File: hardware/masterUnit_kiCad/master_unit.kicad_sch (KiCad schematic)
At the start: 13 parts, among them IC1 THVD8000DDFR, J1 Conn_01x03, J2 Conn_01x02, U1 DEV-15583

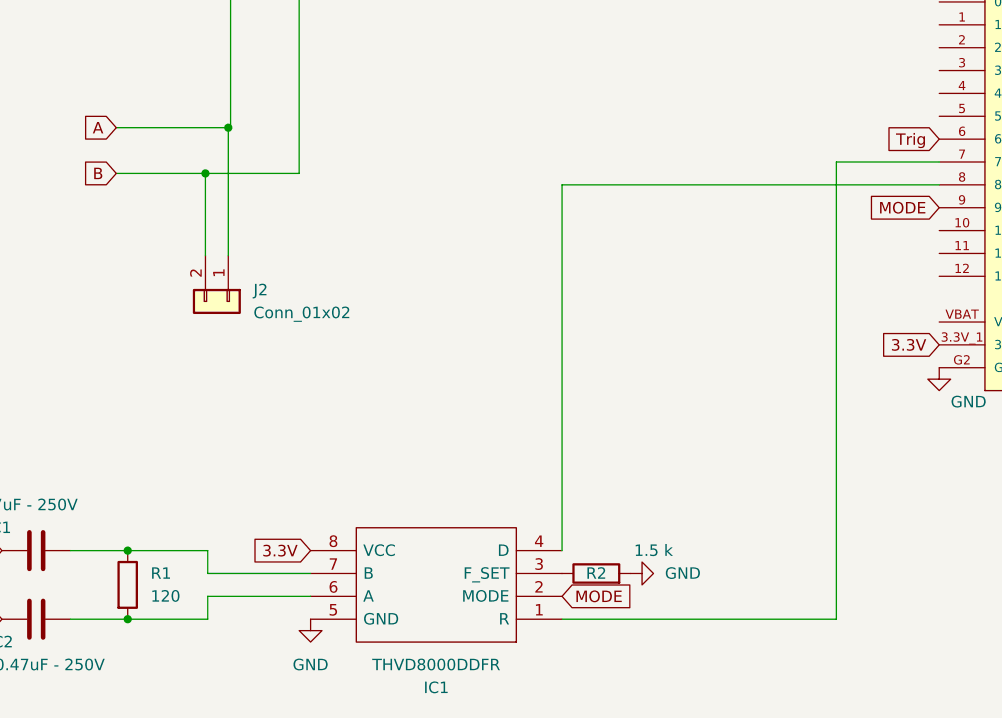
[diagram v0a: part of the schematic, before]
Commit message: Added LED to the master board
BLUE for power
RED for receiving data
GREEN for sending data
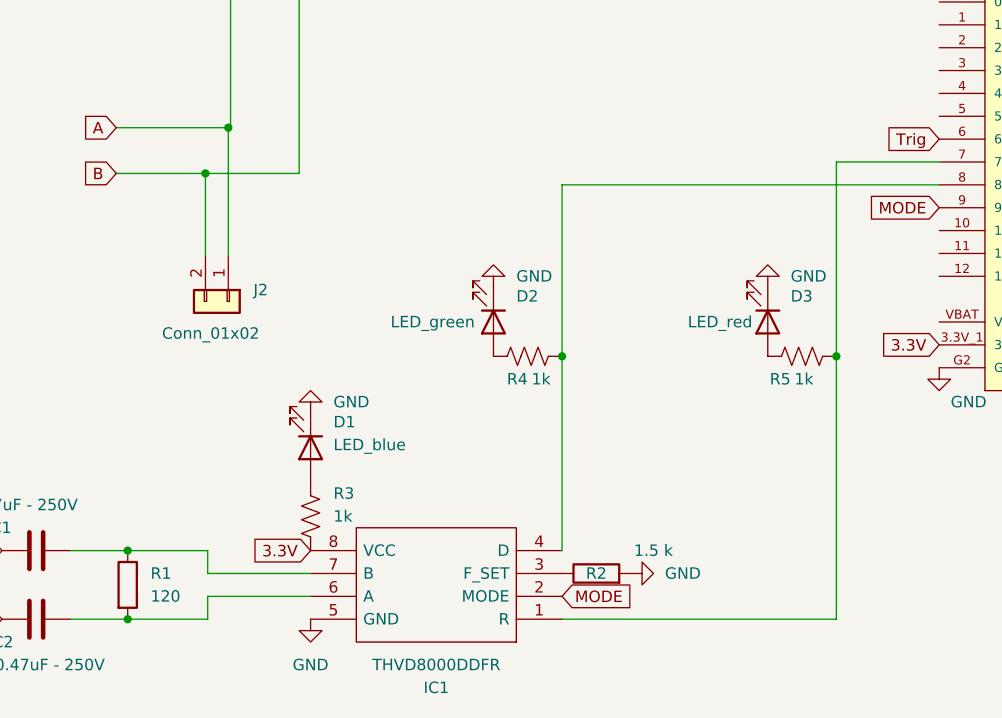
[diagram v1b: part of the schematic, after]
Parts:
- added D1: LED_blue, LED_SMD:LED_1206_3216Metric, symbol Device:LED
- added D2: LED_green, LED_SMD:LED_1206_3216Metric, symbol Device:LED
- added D3: LED_red, LED_SMD:LED_1206_3216Metric, symbol Device:LED
- added R3, R4, R5: 1k, Resistor_SMD:R_1206_3216Metric, symbol Device:R_US
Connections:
- net 3.3V: now also R3.2
- net GND: now also D1.1 (K), D2.1 (K), D3.1 (K)
- net at IC1.1 (R), U1.7: now also R5.2
- net at IC1.4 (D), U1.8: now also R4.2
- new net: D2.2 (A), R4.1
- new net: D3.2 (A), R5.1
- new net: D1.2 (A), R3.1

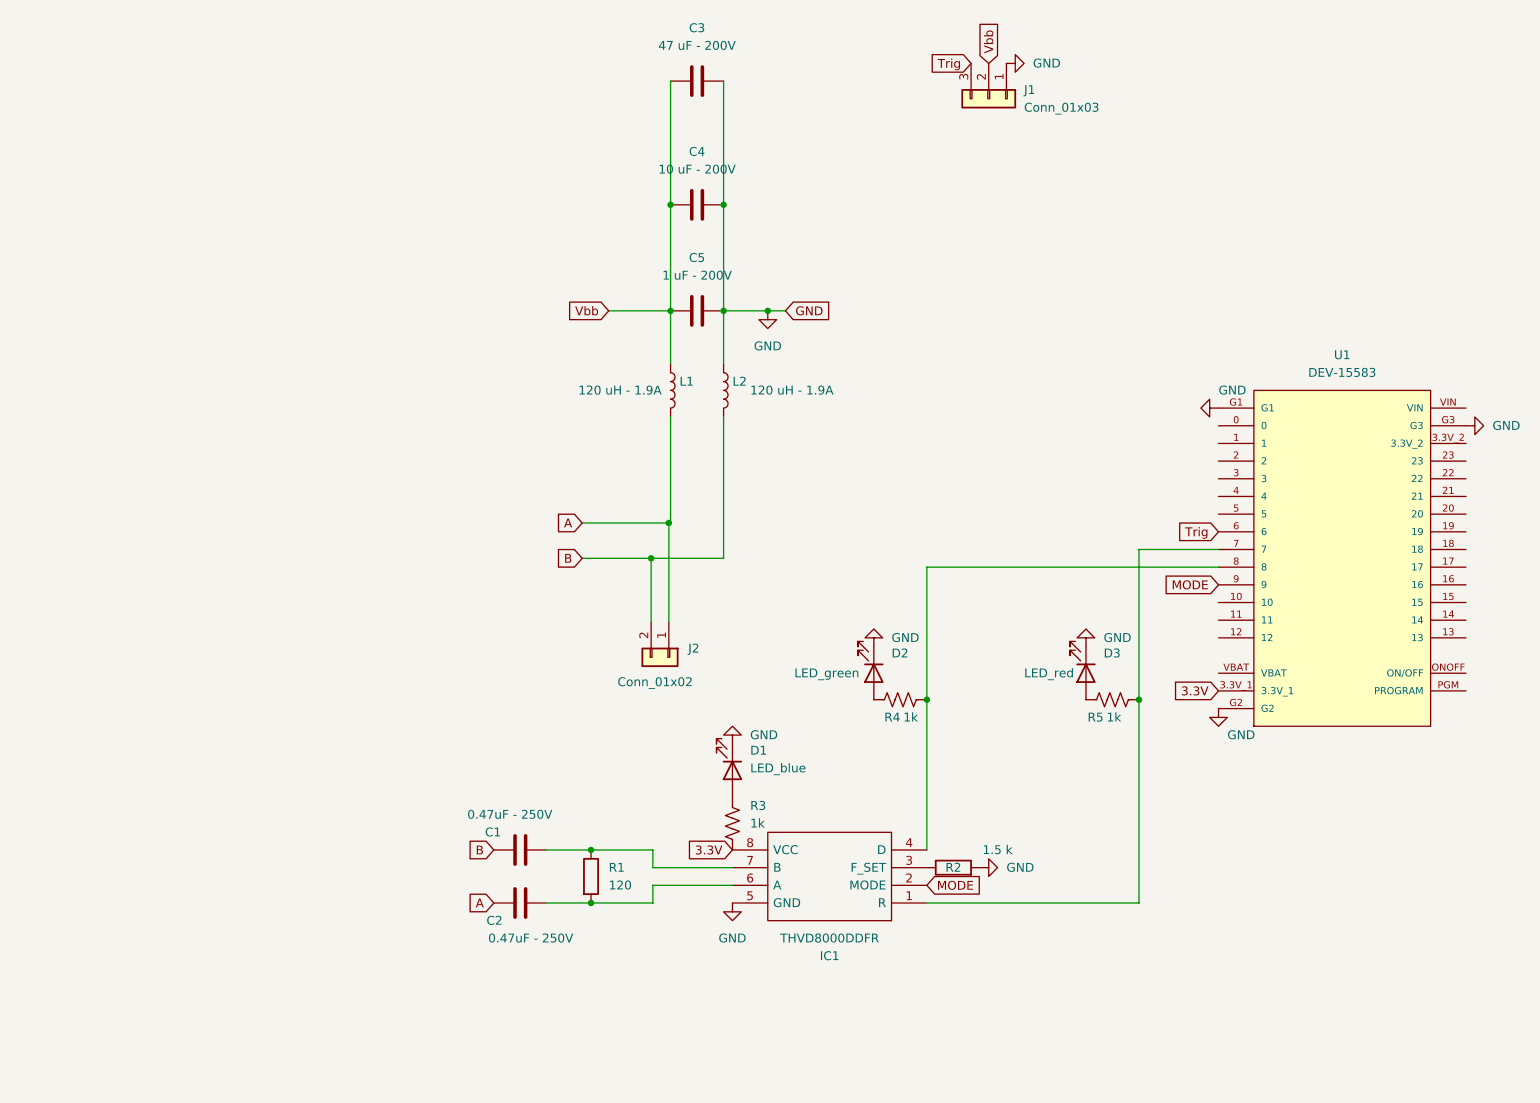
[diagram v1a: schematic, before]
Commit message: updated pcb layout with new LED
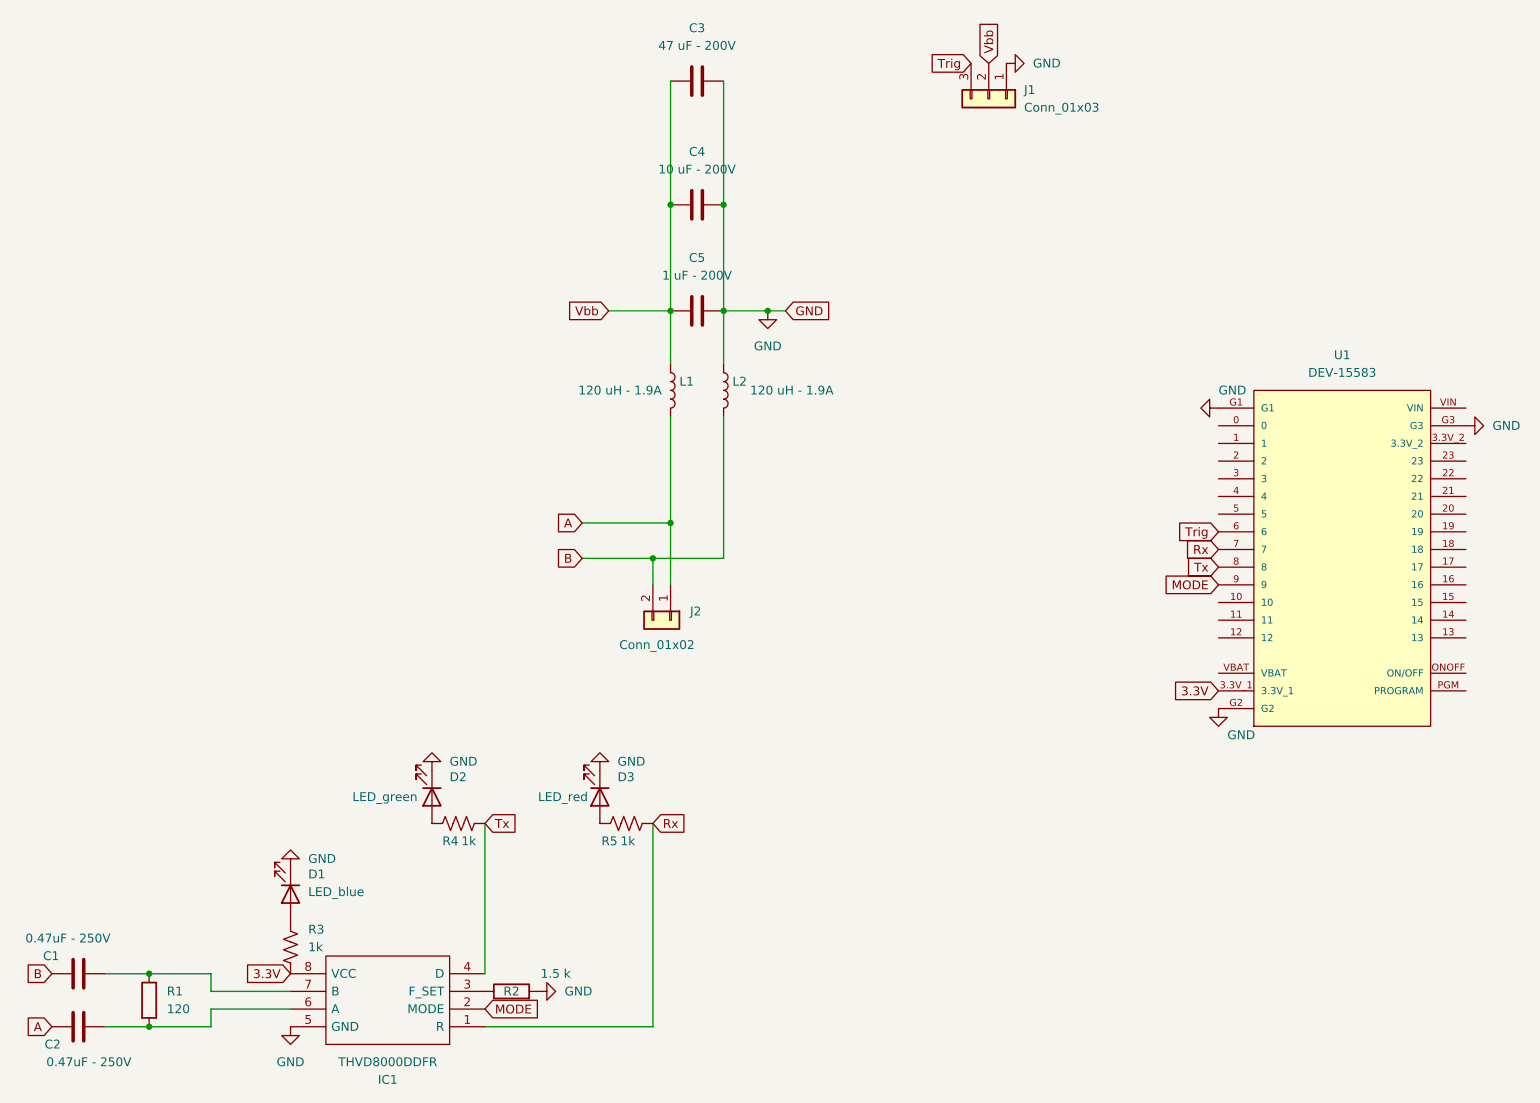
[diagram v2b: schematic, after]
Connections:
- net Rx: now reaches IC1.1 (R), R5.2, U1.7
- net Tx: now reaches IC1.4 (D), R4.2, U1.8
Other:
- moved on the sheet: C1, C2, D1, D2, D3, IC1, J2, R1, R2, R3, R4, R5
